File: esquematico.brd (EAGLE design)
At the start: 200 x 139.8 mm, 5 parts, among them U1 ROB-14450

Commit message: Create DRV8833 Lib
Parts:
- added U$2: DRV8833, DRV8833:DRV8833
- added X2, X3: (no value), con-ptr500:AK300/2
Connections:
- new net N$1: X2.1
- new net N$3: X2.2
- new net N$4: X3.1
- new net N$5: X3.2
- net BL: now also U$1.P$10
- net CE: now also U$1.P$15; no longer U$1.P$14
- net CLK: now also U$1.P$11; no longer U$1.P$17
- net DC: now also U$1.P$14; no longer U$1.P$15
- net DIN: now also U$1.P$13; no longer U$1.P$16
- net RST: now also U$1.P$16; no longer U$1.P$13
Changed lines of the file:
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@@
 <attribute name="VALUE" x="71.12" y="30.734" size="1.778" layer="27" ratio="10"/>
+</element>
+<element name="X2" library="con-ptr500" library_urn="urn:adsk.eagle:library:181" package="AK300/2" package3d_urn="urn:adsk.eagle:package:9881/1" value="" x="-6.35" y="10.16" smashed="yes">
+<attribute name="MF" value="" x="-6.35" y="10.16" size="1.778" layer="27" display="off"/>
+<attribute name="MPN" value="" x="-6.35" y="10.16" size="1.778" layer="27" display="off"/>
+<attribute name="NAME" x="-11.43" y="16.891" size="1.778" layer="25" ratio="10"/>
+<attribute name="OC_FARNELL" value="unknown" x="-6.35" y="10.16" size="1.778" layer="27" display="off"/>
+<attribute name="OC_NEWARK" value="unknown" x="-6.35" y="10.16" size="1.778" layer="27" display="off"/>
+<attribute name="POPULARITY" value="16" x="-6.35" y="10.16" size="1.778" layer="27" display="off"/>
+<attribute name="VALUE" x="-11.43" y="1.524" size="1.778" layer="27" ratio="10"/>
+</element>
+<element name="X3" library="con-ptr500" library_urn="urn:adsk.eagle:library:181" package="AK300/2" package3d_urn="urn:adsk.eagle:package:9881/1" value="" x="-17.78" y="10.16" smashed="yes">
+<attribute name="MF" value="" x="-17.78" y="10.16" size="1.778" layer="27" display="off"/>
+<attribute name="MPN" value="" x="-17.78" y="10.16" size="1.778" layer="27" display="off"/>
+<attribute name="NAME" x="-22.86" y="16.891" size="1.778" layer="25" ratio="10"/>
+<attribute name="OC_FARNELL" value="unknown" x="-17.78" y="10.16" size="1.778" layer="27" display="off"/>
+<attribute name="OC_NEWARK" value="unknown" x="-17.78" y="10.16" size="1.778" layer="27" display="off"/>
+<attribute name="POPULARITY" value="16" x="-17.78" y="10.16" size="1.778" layer="27" display="off"/>
+<attribute name="VALUE" x="-22.86" y="1.524" size="1.778" layer="27" ratio="10"/>
+</element>
+<element name="U$2" library="DRV8833" package="DRV8833" value="DRV8833" x="170.18" y="24.13" smashed="yes">
+<attribute name="NAME" x="157.6618" y="38.9182" size="1.27" layer="25"/>
+<attribute name="VALUE" x="157.6618" y="16.9618" size="1.27" layer="27" align="top-left"/>
 </element>
 </elements>
@@
 <signal name="RST">
 <contactref element="DISPLAY" pad="1"/>
-<contactref element="U$1" pad="P$13"/>
-<wire x1="38.1" y1="31.75" x2="93.98" y2="106.68" width="0" layer="19" extent="1-1"/>
+<contactref element="U$1" pad="P$16"/>
+<wire x1="38.1" y1="24.13" x2="93.98" y2="106.68" width="0" layer="19" extent="1-1"/>
 </signal>
 <signal name="CE">
 <contactref element="DISPLAY" pad="2"/>
-<contactref element="U$1" pad="P$14"/>
-<wire x1="38.1" y1="29.21" x2="96.52" y2="106.68" width="0" layer="19" extent="1-1"/>
+<contactref element="U$1" pad="P$15"/>
+<wire x1="38.1" y1="26.67" x2="96.52" y2="106.68" width="0" layer="19" extent="1-1"/>
 </signal>
 <signal name="DC">
 <contactref element="DISPLAY" pad="3"/>
-<contactref element="U$1" pad="P$15"/>
-<wire x1="38.1" y1="26.67" x2="99.06" y2="106.68" width="0" layer="19" extent="1-1"/>
+<contactref element="U$1" pad="P$14"/>
+<wire x1="38.1" y1="29.21" x2="99.06" y2="106.68" width="0" layer="19" extent="1-1"/>
 </signal>
 <signal name="DIN">
 <contactref element="DISPLAY" pad="4"/>
-<contactref element="U$1" pad="P$16"/>
-<wire x1="38.1" y1="24.13" x2="101.6" y2="106.68" width="0" layer="19" extent="1-1"/>
+<contactref element="U$1" pad="P$13"/>
+<wire x1="38.1" y1="31.75" x2="101.6" y2="106.68" width="0" layer="19" extent="1-1"/>
 </signal>
 <signal name="CLK">
 <contactref element="DISPLAY" pad="5"/>
-<contactref element="U$1" pad="P$17"/>
-<wire x1="38.1" y1="21.59" x2="104.14" y2="106.68" width="0" layer="19" extent="1-1"/>
+<contactref element="U$1" pad="P$11"/>
+<wire x1="38.1" y1="36.83" x2="104.14" y2="106.68" width="0" layer="19" extent="1-1"/>
 </signal>
 <signal name="BL">
 <contactref element="DISPLAY" pad="7"/>
-</signal>
-<signal name="N$6">
-<contactref element="U$1" pad="P$12"/>
+<contactref element="U$1" pad="P$10"/>
+<wire x1="38.1" y1="39.37" x2="109.22" y2="106.68" width="0" layer="19" extent="1-1"/>
 </signal>
 <signal name="+7.4V">
 <contactref element="X1" pad="1"/>
 </signal>
+<signal name="N$2">
+<contactref element="U$1" pad="P$12"/>
+</signal>
+<signal name="N$1">
+<contactref element="X2" pad="1"/>
+</signal>
+<signal name="N$3">
+<contactref element="X2" pad="2"/>
+</signal>
+<signal name="N$4">
+<contactref element="X3" pad="1"/>
+</signal>
+<signal name="N$5">
+<contactref element="X3" pad="2"/>
+</signal>
 </signals>

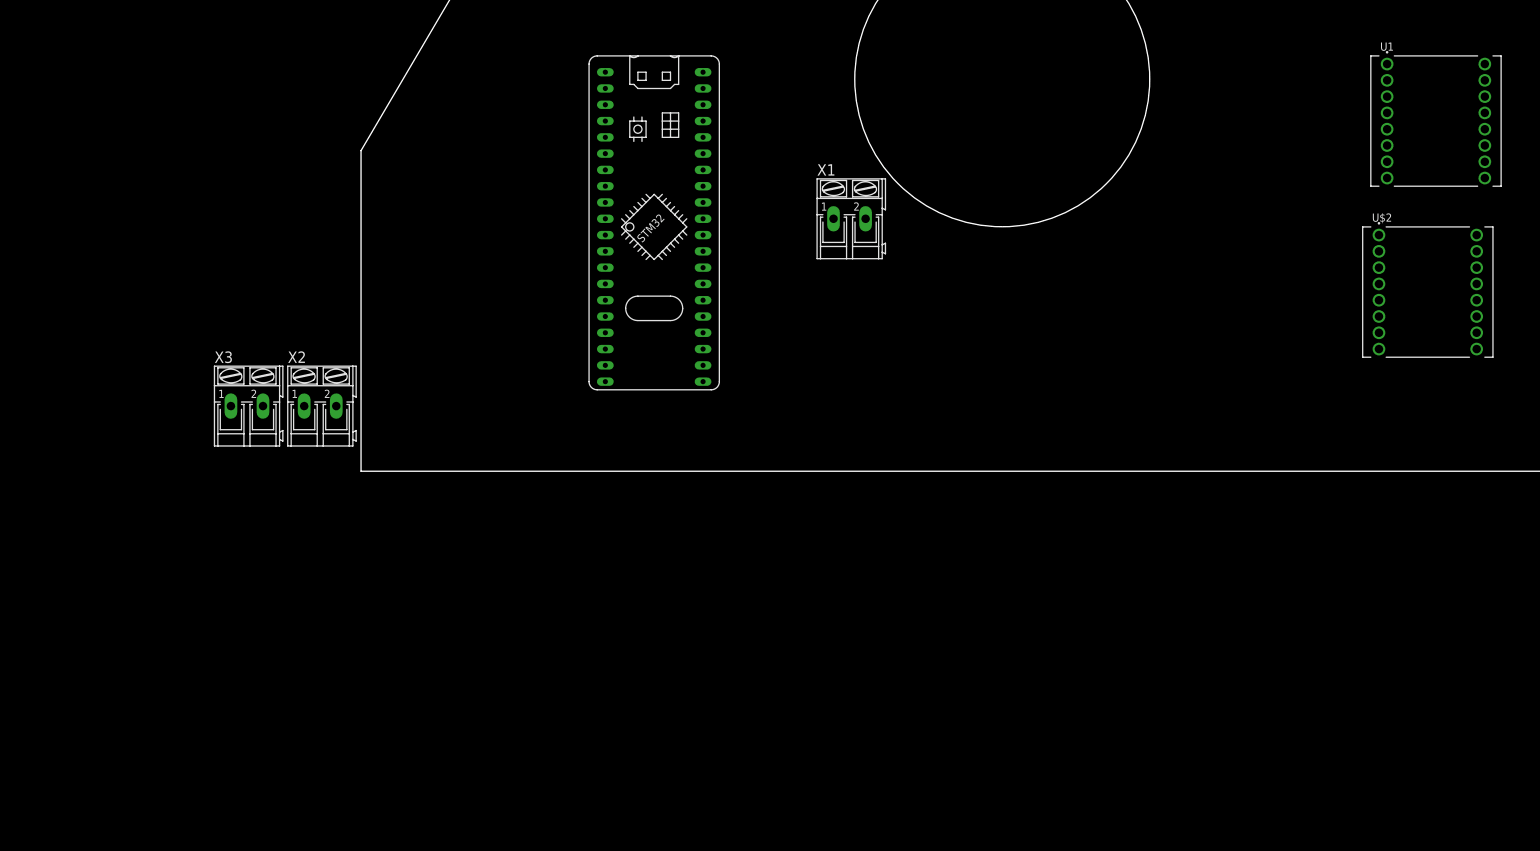
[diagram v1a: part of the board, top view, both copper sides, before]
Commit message: Atualização Pinos STM32 e Lib
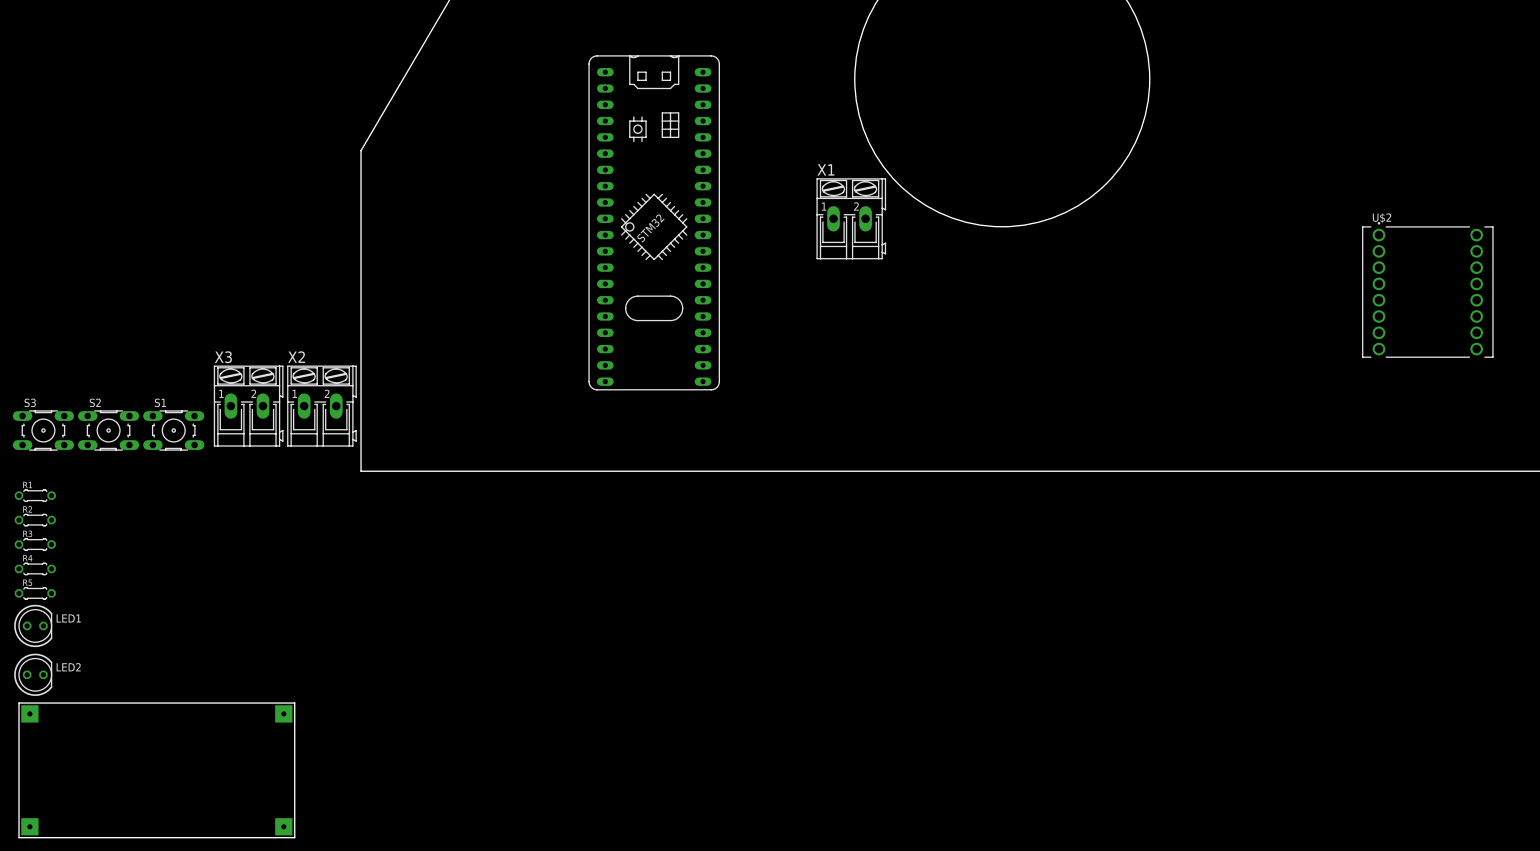
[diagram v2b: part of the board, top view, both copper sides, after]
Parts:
- removed U1: ROB-14450, ROB-14450:MODULE_ROB-14450
- added LED1, LED2: (no value), led:LED5MM
- added R1, R2, R3, R4, R5: (no value), rcl:0204/5
- added S1, S2, S3: (no value), switch-omron:B3F-10XX
- added U$3: LM2596, DRV8833:LM2596
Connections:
- removed net AI1: U$1.P$5, U1.14
- removed net AI2: U$1.P$6, U1.15
- removed net BI1: U$1.P$7, U1.12
- removed net BI2: U$1.P$8, U1.11
- removed net N$3: X2.2
- removed net N$4: X3.1
- removed net N$5: X3.2
- removed net PWMA: U$1.P$2, U1.16
- removed net PWMB: U$1.P$3, U1.10
- removed net PWMC: U$1.P$4
- removed net VM: U1.1
- new net AIN1: U$1.P$6, U$2.11
- new net AIN2: U$1.P$5, U$2.10
- new net BIN1: U$1.P$10, U$2.13
- new net BIN2: U$1.P$11, U$2.14
- new net BOT1: R1.1, S1.1, S1.2, U$1.P$14
- new net BOT2: R2.1, S2.1, S2.2, U$1.P$15
- new net BOT3: R3.1, S3.1, S3.2, U$1.P$16
- new net EN_LED1: R4.1, U$1.P$12
- new net EN_LED2: R5.1, U$1.P$13
- net +7.4V: now also U$3.P$1
- net A01: now also U$2.4, X2.1; no longer U1.4
- net A02: now also U$2.5, X2.2; no longer U1.5
- net B01: now also U$2.7, X3.1; no longer U1.7
- net B02: now also U$2.6, X3.2; no longer U1.6
- net BL: now also U$1.P$31; no longer U$1.P$10
- net CE: now also U$1.P$26; no longer U$1.P$15
- net CLK: now also U$1.P$30; no longer U$1.P$11
- net DC: now also U$1.P$27; no longer U$1.P$14
- net DIN: now also U$1.P$28; no longer U$1.P$13
- net EN: now also U$1.P$38; no longer U$1.P$32
- net GND: now also LED1.K, LED2.K, S1.3, S1.4, S2.3, S2.4, S3.3, S3.4, U$2.16, U$2.3, U$2.8, U$3.P$2, U$3.P$4; no longer U1.3, U1.8, U1.9
- net N$1: now also LED1.A, R4.2; no longer X2.1
- net N$2: now also LED2.A, R5.2; no longer U$1.P$12
- net RST: now also U$1.P$25; no longer U$1.P$16
- net S0: now also U$1.P$37; no longer U$1.P$31
- net S1: now also U$1.P$35; no longer U$1.P$30
- net S2: now also U$1.P$34; no longer U$1.P$29
- net S3: now also U$1.P$33; no longer U$1.P$28
- net SIG: now also U$1.P$32; no longer U$1.P$27
- net STBY: now also U$1.P$8, U$2.12; no longer U$1.P$9, U1.13
- net VCC: now also R1.2, R2.2, R3.2, U$2.1, U$3.P$3; no longer U1.2
